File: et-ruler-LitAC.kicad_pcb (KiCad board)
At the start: 2 copper layers, 166 x 28 mm, 27 parts, among them J1 Conn_01x03, J3 Pmod-Interface-GPIO6, J4 Pmod-Interface-GPIO6, J5 AudioJack3_SwitchTR, SW1 SW_DPDT, U1 OP07

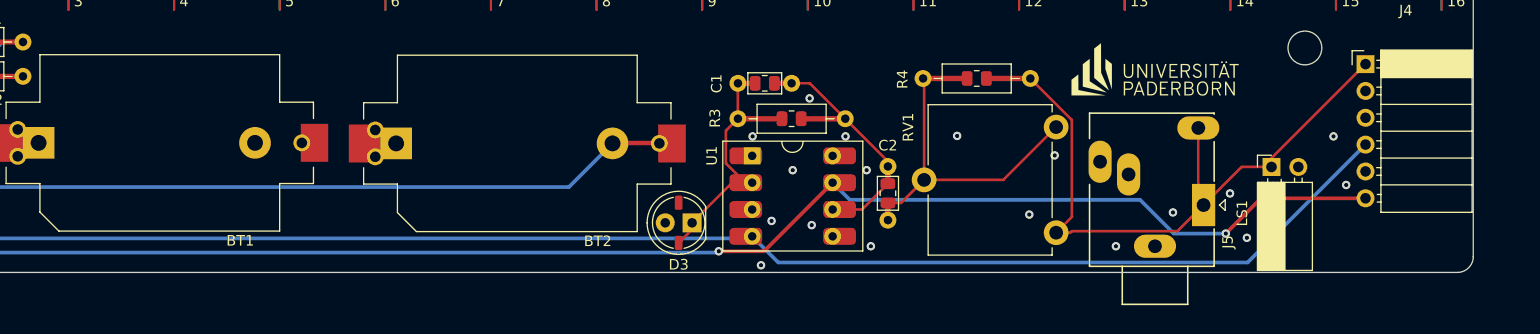
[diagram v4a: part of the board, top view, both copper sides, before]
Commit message: Add text, labels, and version number
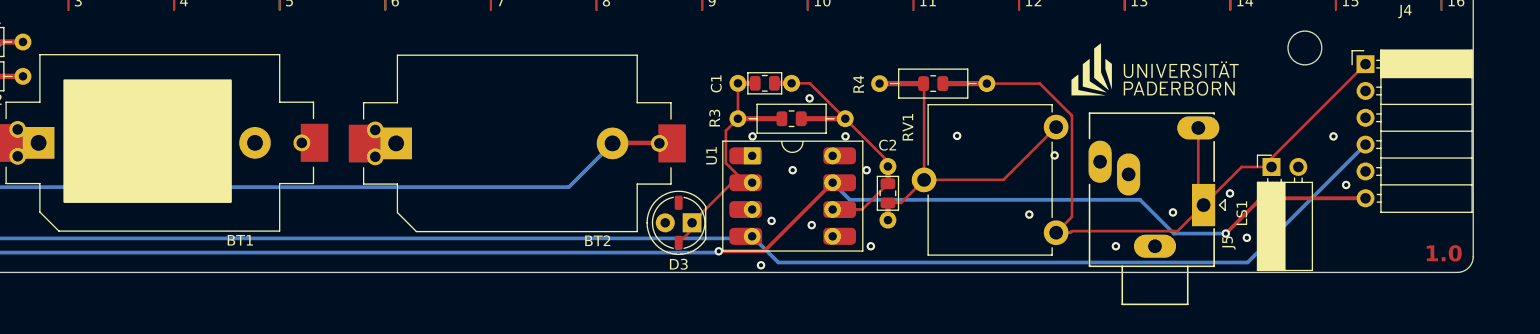
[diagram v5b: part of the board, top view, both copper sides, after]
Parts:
- moved R4 4.15 mm to (163.9, 71.3)
- moved QR1 0.95 mm to (89.6, 76.2)
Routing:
- net amp_out: track 60.7 -> 64.9 mm
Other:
- board text added: "1.0"
- board text added: "Institut für Elektrotechnik und Informationstechnik ei.uni-paderborn.de"
- board text added: "Name"
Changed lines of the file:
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@@
     (fp_arc (start 1.8 -1.4) (mid 2.103203 -1.266503) (end 2.3 -1)
       (stroke (width 0.12) (type solid)) (layer "F.SilkS"))
-    (fp_arc (start 2.31113 1.079837) (mid 2.072239 1.266536) (end 1.8 1.4)
+    (fp_arc (start 2.31113 1.079837) (mid 2.072238 1.266535) (end 1.8 1.4)
       (stroke (width 0.12) (type solid)) (layer "F.SilkS"))
     (fp_arc (start 2.942335 1.078608) (mid 2.427699 1.61666) (end 1.75 1.925)
@@
     (fp_arc (start -0.29 -1.235516) (mid 0.17605 -1.661635) (end 0.75 -1.925)
       (stroke (width 0.12) (type solid)) (layer "F.SilkS"))
-    (fp_arc (start 0.229039 -1.08) (mid 0.493915 -1.276765) (end 0.8 -1.4)
+    (fp_arc (start 0.229039 -1.08) (mid 0.493915 -1.276764) (end 0.8 -1.4)
       (stroke (width 0.12) (type solid)) (layer "F.SilkS"))
     (fp_arc (start 0.7 1.399999) (mid 0.416313 1.240602) (end 0.172957 1.024584)
@@
     (fp_arc (start 1.8 -1.4) (mid 2.07224 -1.266539) (end 2.31113 -1.079837)
       (stroke (width 0.12) (type solid)) (layer "F.SilkS"))
-    (fp_arc (start 2.31113 1.079837) (mid 2.072238 1.266535) (end 1.8 1.4)
+    (fp_arc (start 2.31113 1.079837) (mid 2.072235 1.266532) (end 1.8 1.4)
       (stroke (width 0.12) (type solid)) (layer "F.SilkS"))
     (fp_arc (start 2.942335 1.078608) (mid 2.41819 1.62337) (end 1.725 1.925)
@@
   )
   (footprint "Resistor_HYBRID-emt:R_0805_THT_10.16mm_Hybrid" (layer "F.Cu")
-    (at 168.021 70.866)
+    (at 163.903125 71.35)
     (descr "Hybrid footprint for 0805 SMD and THT components with a 10.16mm Pitch")
     (tags "SMD THT Hybrid")
@@
   )
   (footprint "Symbol-emt:qr-studiere-et_15x16" (layer "B.Cu")
-    (at 90.551 76.2 180)
+    (at 89.6 76.165 180)
     (property "Sheetfile" "et-ruler-LitAC.kicad_sch")
     (property "Sheetname" "")
@@
       (stroke (width 0.2) (type solid)) (layer "B.Mask"))
   )
+  (gr_rect (start 207.3 66.975) (end 214.8 84.725)
+    (stroke (width 0.2) (type solid)) (fill solid) (layer "B.SilkS"))
+  (gr_rect (start 81.65 71.1) (end 97.4 82.6)
+    (stroke (width 0.2) (type solid)) (fill solid) (layer "F.SilkS"))
   (gr_line (start 215.032 61.278) (end 49.032 61.278)
     (stroke (width 0.1) (type solid)) (layer "Edge.Cuts"))
@@
   (gr_line (start 50.532 89.278) (end 213.532 89.278)
     (stroke (width 0.1) (type solid)) (layer "Edge.Cuts"))
+  (gr_text "1.0" (at 210.4 88.4) (layer "F.Cu" knockout)
+    (effects (font (size 1.5 1.5) (thickness 0.3) bold) (justify left bottom))
+  )
+  (gr_text "Institut für Elektrotechnik und Informationstechnik\nei.uni-paderborn.de" (at 195.4 70.8) (layer "B.SilkS")
+    (effects (font (size 1.5 1.5) (thickness 0.3) bold) (justify left bottom mirror))
+  )
+  (gr_text "Name" (at 212.8 85.6) (layer "B.SilkS")
+    (effects (font (size 1 1) (thickness 0.1)) (justify mirror))
+  )
   (dimension (type aligned) (layer "F.Cu")
     (pts (xy 52.032 61.4172) (xy 212.032 61.4172))
@@
   (segment (start 53.232 82.258) (end 59.222 76.268) (width 0.35) (layer "B.Cu") (net 13))
   (segment (start 59.222 76.268) (end 59.222 75.946) (width 0.35) (layer "B.Cu") (net 13))
+  (segment (start 177.036 74.436) (end 174 71.4) (width 0.25) (layer "F.Cu") (net 14))
   (segment (start 189 75.6) (end 189 82.4) (width 0.25) (layer "F.Cu") (net 14))
   (segment (start 189.5 82.9) (end 193.107 79.293) (width 0.25) (layer "F.Cu") (net 14))
-  (segment (start 173.101 70.916) (end 177.036 74.851) (width 0.25) (layer "F.Cu") (net 14))
   (segment (start 189 82.4) (end 189.5 82.9) (width 0.25) (layer "F.Cu") (net 14))
-  (segment (start 177.036 74.851) (end 177.036 84.023) (width 0.25) (layer "F.Cu") (net 14))
+  (segment (start 177.036 84.023) (end 177.036 74.436) (width 0.25) (layer "F.Cu") (net 14))
+  (segment (start 174 71.4) (end 168.983125 71.4) (width 0.25) (layer "F.Cu") (net 14))
   (segment (start 175.541 85.518) (end 176.882 85.518) (width 0.25) (layer "F.Cu") (net 14))
-  (segment (start 177.036 84.023) (end 175.541 85.518) (width 0.25) (layer "F.Cu") (net 14))
   (segment (start 177.025 85.375) (end 187.025 85.375) (width 0.25) (layer "F.Cu") (net 14))
   (segment (start 176.882 85.518) (end 177.025 85.375) (width 0.25) (layer "F.Cu") (net 14))
@@
   (segment (start 187.025 85.375) (end 189.5 82.9) (width 0.25) (layer "F.Cu") (net 14))
   (segment (start 193.107 79.293) (end 195.931 79.293) (width 0.25) (layer "F.Cu") (net 14))
+  (segment (start 175.541 85.518) (end 177.036 84.023) (width 0.25) (layer "F.Cu") (net 14))
   (segment (start 195.931 78.459) (end 204.832 69.558) (width 0.25) (layer "F.Cu") (net 14))
   (segment (start 155.0419 83.322) (end 157.169 83.322) (width 0.25) (layer "F.Cu") (net 19))
@@
   (segment (start 150.495 71.374) (end 152.223 71.374) (width 0.25) (layer "F.Cu") (net 19))
   (segment (start 159.6155 78.7665) (end 159.6155 79.248) (width 0.25) (layer "F.Cu") (net 19))
-  (segment (start 163.041 80.518) (end 163.041 71.016) (width 0.25) (layer "F.Cu") (net 23))
+  (segment (start 163.041 80.518) (end 163.041 71.450375) (width 0.25) (layer "F.Cu") (net 23))
+  (segment (start 163.041 71.450375) (end 162.990625 71.4) (width 0.25) (layer "F.Cu") (net 23))
   (segment (start 159.6155 82.7005) (end 160.8585 82.7005) (width 0.25) (layer "F.Cu") (net 23))
   (segment (start 163.041 80.518) (end 170.541 80.518) (width 0.25) (layer "F.Cu") (net 23))

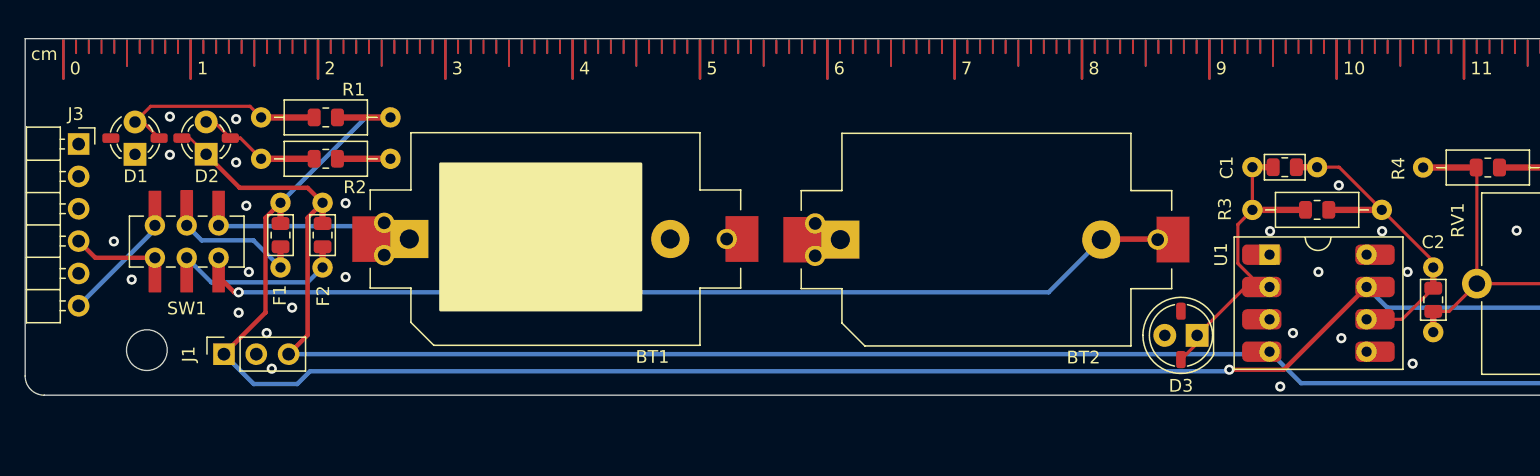
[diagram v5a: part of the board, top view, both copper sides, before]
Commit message: Fix margin around switch
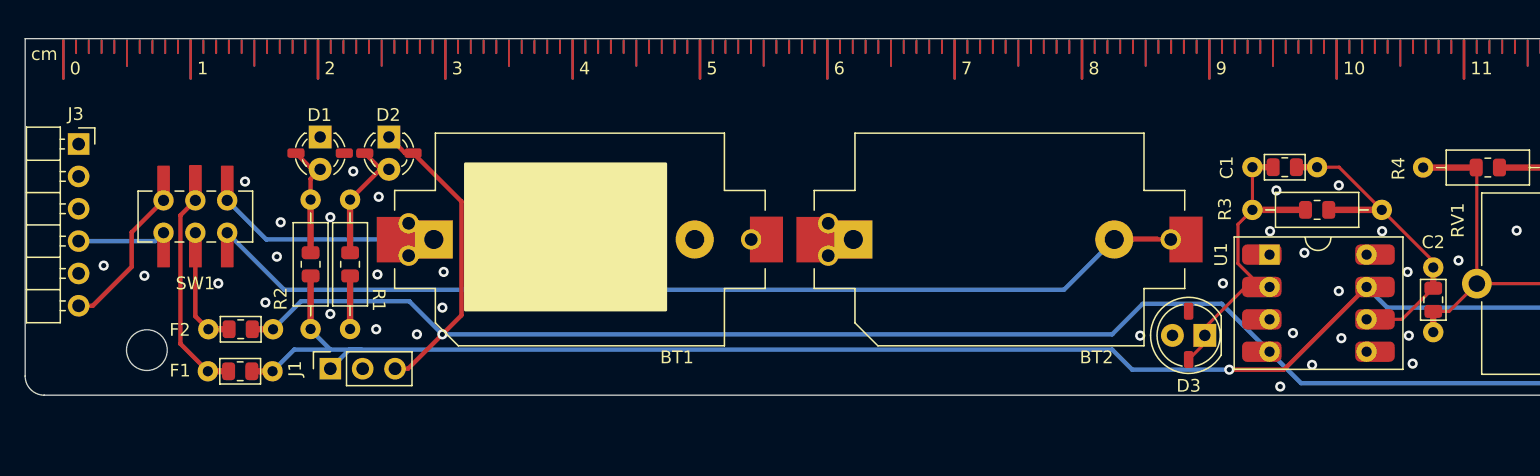
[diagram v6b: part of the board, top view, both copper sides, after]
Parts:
- R1, R2: value R -> 100
- moved D1 14.6 mm to (72.2, 69.0), turned to -90 degrees
- moved D2 14.4 mm to (77.6, 69.0), turned to -90 degrees
- moved R1 11.6 mm to (71.4, 79.0), turned to 90 degrees
- moved F1 11.2 mm to (65.9, 87.4), turned to 0 degrees
- moved F2 9.80 mm to (66.0, 84.1), turned to 0 degrees
- moved R2 8.44 mm to (74.5, 79.0), turned to 90 degrees
- moved J1 8.44 mm to (73.0, 87.2)
- moved SW1 2.08 mm to (62.4, 75.2)
- moved BT1 1.92 mm to (92.6, 77.0)
- moved QR1 1.78 mm to (91.4, 76.2)
- moved BT2 1.02 mm to (125.5, 77.0)
- moved D3 0.60 mm to (141.7, 84.6)
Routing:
- net V+: track 175.4 -> 149.1 mm
- net Net-(D1-A): track 13.2 -> 5.12 mm
- net Net-(SW1-B): track 8.73 -> 14.8 mm
- net Net-(SW1-E): track 12.0 -> 6.52 mm
- net V+_ext_in: track 8.79 -> 11.7 mm
- net Net-(BT2--): track 81.1 -> 83.0 mm, vias 1 -> 0
- net Net-(BT1-+): track 17.3 -> 19.0 mm
- net V-: track 169.3 -> 170.2 mm, vias 0 -> 1
- net Net-(D2-A): track 5.52 -> 6.46 mm
- net GND: vias 32 -> 41

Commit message: Add text
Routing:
- net GND: vias 41 -> 48
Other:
- board text added: "Bat."
- board text added: "Ext."
- board text added: "LitAC"
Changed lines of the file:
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@@
     (effects (font (size 1 1) (thickness 0.1)) (justify mirror))
+  )
+  (gr_text "LitAC" (at 105.2 69.6) (layer "F.SilkS")
+    (effects (font (size 2 2) (thickness 0.3)) (justify left bottom))
+  )
+  (gr_text "Ext." (at 57.1 68.8) (layer "F.SilkS")
+    (effects (font (size 1 1) (thickness 0.15)) (justify left bottom))
+  )
+  (gr_text "Bat." (at 65 68.8) (layer "F.SilkS")
+    (effects (font (size 1 1) (thickness 0.15)) (justify left bottom))
   )
   (dimension (type aligned) (layer "Dwgs.User")
@@
   (via (at 150.1 86.9) (size 0.8) (drill 0.4) (layers "F.Cu" "B.Cu") (free) (net 2))
   (via (at 166.1668 76.3524) (size 0.8) (drill 0.4) (layers "F.Cu" "B.Cu") (free) (net 2))
+  (via (at 134 81.3) (size 0.8) (drill 0.4) (layers "F.Cu" "B.Cu") (free) (net 2))
   (via (at 66.3 72.5) (size 0.8) (drill 0.4) (layers "F.Cu" "B.Cu") (free) (net 2))
   (via (at 81.8 82.4) (size 0.8) (drill 0.4) (layers "F.Cu" "B.Cu") (free) (net 2))
@@
   (via (at 73 75.3) (size 0.8) (drill 0.4) (layers "F.Cu" "B.Cu") (free) (net 2))
   (via (at 152.2 81.1) (size 0.8) (drill 0.4) (layers "F.Cu" "B.Cu") (free) (net 2))
+  (via (at 104.8 83) (size 0.8) (drill 0.4) (layers "F.Cu" "B.Cu") (free) (net 2))
   (via (at 73 82.9) (size 0.8) (drill 0.4) (layers "F.Cu" "B.Cu") (free) (net 2))
+  (via (at 80.8 87.7) (size 0.8) (drill 0.4) (layers "F.Cu" "B.Cu") (free) (net 2))
   (via (at 143.1 80.5) (size 0.8) (drill 0.4) (layers "F.Cu" "B.Cu") (free) (net 2))
   (via (at 81.9 79.6) (size 0.8) (drill 0.4) (layers "F.Cu" "B.Cu") (free) (net 2))
+  (via (at 61.6 88.5) (size 0.8) (drill 0.4) (layers "F.Cu" "B.Cu") (free) (net 2))
   (via (at 74.8 71.7) (size 0.8) (drill 0.4) (layers "F.Cu" "B.Cu") (free) (net 2))
+  (via (at 64.3 85.7) (size 0.8) (drill 0.4) (layers "F.Cu" "B.Cu") (free) (net 2))
   (via (at 69.1 75.7) (size 0.8) (drill 0.4) (layers "F.Cu" "B.Cu") (free) (net 2))
   (via (at 136.6 84.6) (size 0.8) (drill 0.4) (layers "F.Cu" "B.Cu") (free) (net 2))
@@
   (via (at 157.6 79.6) (size 0.8) (drill 0.4) (layers "F.Cu" "B.Cu") (free) (net 2))
   (via (at 192 81.8) (size 0.8) (drill 0.4) (layers "F.Cu" "B.Cu") (free) (net 2))
+  (via (at 70.3 88.4) (size 0.8) (drill 0.4) (layers "F.Cu" "B.Cu") (free) (net 2))
   (via (at 173 83.8) (size 0.8) (drill 0.4) (layers "F.Cu" "B.Cu") (free) (net 2))
   (via (at 149.5 78.1) (size 0.8) (drill 0.4) (layers "F.Cu" "B.Cu") (free) (net 2))
   (via (at 146.8 76.4) (size 0.8) (drill 0.4) (layers "F.Cu" "B.Cu") (free) (net 2))
   (via (at 152.4 84.8) (size 0.8) (drill 0.4) (layers "F.Cu" "B.Cu") (free) (net 2))
+  (via (at 113.5 82.9) (size 0.8) (drill 0.4) (layers "F.Cu" "B.Cu") (free) (net 2))
   (via (at 147.3 73.2) (size 0.8) (drill 0.4) (layers "F.Cu" "B.Cu") (free) (net 2))
   (via (at 64.2 80.5) (size 0.8) (drill 0.4) (layers "F.Cu" "B.Cu") (free) (net 2))
@@
   (segment (start 76.93 71.54) (end 77.6 71.54) (width 0.35) (layer "F.Cu") (net 8))
   (segment (start 76.97 71.54) (end 75.7 70.27) (width 0.35) (layer "F.Cu") (net 8))
+  (segment (start 63.38 86.58) (end 61.225 84.425) (width 0.35) (layer "F.Cu") (net 9))
   (segment (start 61.225 75.155) (end 62.4 73.98) (width 0.35) (layer "F.Cu") (net 9))
-  (segment (start 61.225 85.245) (end 61.225 75.155) (width 0.35) (layer "F.Cu") (net 9))
-  (segment (start 63.38 87.4) (end 61.225 85.245) (width 0.35) (layer "F.Cu") (net 9))
+  (segment (start 63.38 87.4) (end 63.38 86.58) (width 0.35) (layer "F.Cu") (net 9))
+  (segment (start 61.225 84.425) (end 61.225 75.155) (width 0.35) (layer "F.Cu") (net 9))
   (segment (start 62.4 83.08) (end 63.42 84.1) (width 0.35) (layer "F.Cu") (net 10))
   (segment (start 62.4 78) (end 62.4 83.08) (width 0.35) (layer "F.Cu") (net 10))
